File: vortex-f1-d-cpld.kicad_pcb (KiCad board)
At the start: 2 copper layers, 80 x 50 mm, 46 parts, among them J1 JTAG, U1 FDC 9229, U2 XC9572XL, U3 AZ1117-3.3, U4 uPD765AC, U5 AM29F010, U6 74LS06N, U7 SN74LS07N, U8 74LS06N, X1 8Mhz

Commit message: tweaks
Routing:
- net A0: track 91.3 -> 92.6 mm
- net WGATE: track 30.8 -> 31.3 mm
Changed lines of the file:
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@@
   (segment (start 148.69163 133.2072) (end 148.321644 132.837214) (width 0.2) (layer "F.Cu") (net 12))
   (segment (start 169.1386 137.3378) (end 168.8846 137.0838) (width 0.2) (layer "F.Cu") (net 12))
-  (segment (start 170.688 115.1128) (end 178.3588 115.1128) (width 0.2) (layer "F.Cu") (net 12))
-  (segment (start 170.2562 115.5446) (end 170.688 115.1128) (width 0.2) (layer "F.Cu") (net 12))
-  (segment (start 178.3588 115.1128) (end 178.6382 114.8334) (width 0.2) (layer "F.Cu") (net 12))
   (segment (start 148.321644 132.837214) (end 129.586014 132.837214) (width 0.2) (layer "F.Cu") (net 12))
   (segment (start 168.8846 137.0838) (end 165.9382 137.0838) (width 0.2) (layer "F.Cu") (net 12))
   (segment (start 163.108248 133.2072) (end 148.69163 133.2072) (width 0.2) (layer "F.Cu") (net 12))
+  (segment (start 178.4008 115.0708) (end 178.6382 114.8334) (width 0.2) (layer "F.Cu") (net 12))
+  (segment (start 169.3926 114.7572) (end 169.5784 114.5714) (width 0.2) (layer "F.Cu") (net 12))
+  (segment (start 176.660552 115.0708) (end 178.4008 115.0708) (width 0.2) (layer "F.Cu") (net 12))
+  (segment (start 176.161152 114.5714) (end 176.660552 115.0708) (width 0.2) (layer "F.Cu") (net 12))
   (segment (start 165.603 137.419) (end 165.603 138.171) (width 0.2) (layer "F.Cu") (net 12))
+  (segment (start 169.5784 114.5714) (end 176.161152 114.5714) (width 0.2) (layer "F.Cu") (net 12))
   (segment (start 168.548 133.458) (end 163.359048 133.458) (width 0.2) (layer "F.Cu") (net 12))
   (segment (start 165.9382 137.0838) (end 165.603 137.419) (width 0.2) (layer "F.Cu") (net 12))
@@
   (via (at 178.6382 114.8334) (size 0.5) (drill 0.3) (layers "F.Cu" "B.Cu") (net 12))
   (via (at 169.037 132.969) (size 0.5) (drill 0.3) (layers "F.Cu" "B.Cu") (net 12))
-  (via (at 170.2562 115.5446) (size 0.5) (drill 0.3) (layers "F.Cu" "B.Cu") (net 12))
+  (via (at 169.3926 114.7572) (size 0.5) (drill 0.3) (layers "F.Cu" "B.Cu") (net 12))
   (segment (start 178.158 108.096308) (end 178.457908 107.7964) (width 0.2) (layer "B.Cu") (net 12))
   (segment (start 178.457908 107.7964) (end 179.1225 107.7964) (width 0.2) (layer "B.Cu") (net 12))
-  (segment (start 170.2562 115.5446) (end 169.127242 116.673558) (width 0.2) (layer "B.Cu") (net 12))
   (segment (start 169.0878 133.0198) (end 169.037 132.969) (width 0.2) (layer "B.Cu") (net 12))
   (segment (start 178.158 108.496492) (end 178.158 108.096308) (width 0.2) (layer "B.Cu") (net 12))
-  (segment (start 169.691704 132.288896) (end 169.2402 132.7404) (width 0.2) (layer "B.Cu") (net 12))
+  (segment (start 169.472 124.89904) (end 169.472 125.869488) (width 0.2) (layer "B.Cu") (net 12))
   (segment (start 178.5398 108.878292) (end 178.158 108.496492) (width 0.2) (layer "B.Cu") (net 12))
-  (segment (start 169.472 124.89904) (end 169.472 125.869488) (width 0.2) (layer "B.Cu") (net 12))
+  (segment (start 169.3926 114.7572) (end 169.127242 115.022558) (width 0.2) (layer "B.Cu") (net 12))
+  (segment (start 169.691704 126.089192) (end 169.691704 132.288896) (width 0.2) (layer "B.Cu") (net 12))
+  (segment (start 169.127242 117.209642) (end 169.320242 117.402642) (width 0.2) (layer "B.Cu") (net 12))
+  (segment (start 169.320242 117.402642) (end 169.320242 124.747282) (width 0.2) (layer "B.Cu") (net 12))
+  (segment (start 169.472 125.869488) (end 169.691704 126.089192) (width 0.2) (layer "B.Cu") (net 12))
   (segment (start 169.2402 132.7404) (end 169.2402 133.0198) (width 0.2) (layer "B.Cu") (net 12))
   (segment (start 169.3316 137.1448) (end 169.3316 136.116848) (width 0.2) (layer "B.Cu") (net 12))
   (segment (start 178.5398 114.735) (end 178.5398 108.878292) (width 0.2) (layer "B.Cu") (net 12))
-  (segment (start 169.127242 116.673558) (end 169.127242 117.209642) (width 0.2) (layer "B.Cu") (net 12))
-  (segment (start 169.320242 124.747282) (end 169.472 124.89904) (width 0.2) (layer "B.Cu") (net 12))
   (segment (start 178.6382 114.8334) (end 178.5398 114.735) (width 0.2) (layer "B.Cu") (net 12))
   (segment (start 178.4096 115.062) (end 178.4096 116.8146) (width 0.2) (layer "B.Cu") (net 12))
   (segment (start 169.3316 136.116848) (end 169.2402 136.025448) (width 0.2) (layer "B.Cu") (net 12))
+  (segment (start 169.691704 132.288896) (end 169.2402 132.7404) (width 0.2) (layer "B.Cu") (net 12))
   (segment (start 178.4096 116.8146) (end 179.3494 117.7544) (width 0.2) (layer "B.Cu") (net 12))
   (segment (start 169.2402 136.025448) (end 169.2402 133.0198) (width 0.2) (layer "B.Cu") (net 12))
@@
   (segment (start 169.1386 137.3378) (end 169.3316 137.1448) (width 0.2) (layer "B.Cu") (net 12))
   (segment (start 169.2402 133.0198) (end 169.0878 133.0198) (width 0.2) (layer "B.Cu") (net 12))
-  (segment (start 169.320242 117.402642) (end 169.320242 124.747282) (width 0.2) (layer "B.Cu") (net 12))
-  (segment (start 169.127242 117.209642) (end 169.320242 117.402642) (width 0.2) (layer "B.Cu") (net 12))
-  (segment (start 169.472 125.869488) (end 169.691704 126.089192) (width 0.2) (layer "B.Cu") (net 12))
-  (segment (start 169.691704 126.089192) (end 169.691704 132.288896) (width 0.2) (layer "B.Cu") (net 12))
+  (segment (start 169.127242 115.022558) (end 169.127242 117.209642) (width 0.2) (layer "B.Cu") (net 12))
+  (segment (start 169.320242 124.747282) (end 169.472 124.89904) (width 0.2) (layer "B.Cu") (net 12))
   (segment (start 133.6682 136.767) (end 154.307 136.767) (width 0.2) (layer "F.Cu") (net 13))
   (segment (start 133.4516 136.5504) (end 133.6682 136.767) (width 0.2) (layer "F.Cu") (net 13))
@@
   (segment (start 187.695265 107.576588) (end 187.2964 107.177723) (width 0.2) (layer "B.Cu") (net 89))
   (segment (start 187.5822 105.48704) (end 187.5822 100.0168) (width 0.2) (layer "B.Cu") (net 89))
-  (segment (start 173.7614 110.744) (end 174.0274 110.478) (width 0.2) (layer "F.Cu") (net 90))
-  (segment (start 181.1528 109.9852) (end 186.085892 109.9852) (width 0.2) (layer "F.Cu") (net 90))
-  (segment (start 171.908408 110.744) (end 173.7614 110.744) (width 0.2) (layer "F.Cu") (net 90))
-  (segment (start 168.939395 111.601531) (end 169.239516 111.901652) (width 0.2) (layer "F.Cu") (net 90))
-  (segment (start 169.239516 111.901652) (end 170.4848 111.901652) (width 0.2) (layer "F.Cu") (net 90))
-  (segment (start 170.4848 111.901652) (end 170.774948 111.901652) (width 0.2) (layer "F.Cu") (net 90))
-  (segment (start 186.085892 109.9852) (end 187.283217 108.787875) (width 0.2) (layer "F.Cu") (net 90))
-  (segment (start 171.5262 111.1504) (end 171.5262 111.126208) (width 0.2) (layer "F.Cu") (net 90))
-  (segment (start 180.479192 110.478) (end 180.971992 109.9852) (width 0.2) (layer "F.Cu") (net 90))
-  (segment (start 171.5262 111.126208) (end 171.908408 110.744) (width 0.2) (layer "F.Cu") (net 90))
-  (segment (start 170.774948 111.901652) (end 171.5262 111.1504) (width 0.2) (layer "F.Cu") (net 90))
-  (segment (start 174.0274 110.478) (end 180.479192 110.478) (width 0.2) (layer "F.Cu") (net 90))
-  (segment (start 180.971992 109.9852) (end 181.1528 109.9852) (width 0.2) (layer "F.Cu") (net 90))
+  (segment (start 175.135848 110.1622) (end 169.441 110.1622) (width 0.2) (layer "F.Cu") (net 90))
+  (segment (start 175.141448 110.1566) (end 175.135848 110.1622) (width 0.2) (layer "F.Cu") (net 90))
+  (segment (start 169.441 110.1622) (end 168.939395 110.663805) (width 0.2) (layer "F.Cu") (net 90))
+  (segment (start 186.085892 109.9852) (end 180.971992 109.9852) (width 0.2) (layer "F.Cu") (net 90))
+  (segment (start 180.971992 109.9852) (end 180.505992 110.4512) (width 0.2) (layer "F.Cu") (net 90))
+  (segment (start 180.505992 110.4512) (end 177.762408 110.4512) (width 0.2) (layer "F.Cu") (net 90))
+  (segment (start 177.467808 110.1566) (end 175.141448 110.1566) (width 0.2) (layer "F.Cu") (net 90))
+  (segment (start 187.283217 108.787875) (end 186.085892 109.9852) (width 0.2) (layer "F.Cu") (net 90))
+  (segment (start 168.939395 110.663805) (end 168.939395 111.601531) (width 0.2) (layer "F.Cu") (net 90))
+  (segment (start 177.762408 110.4512) (end 177.467808 110.1566) (width 0.2) (layer "F.Cu") (net 90))
   (via (at 187.283217 108.787875) (size 0.5) (drill 0.3) (layers "F.Cu" "B.Cu") (net 90))
   (via (at 168.939395 111.601531) (size 0.5) (drill 0.3) (layers "F.Cu" "B.Cu") (net 90))

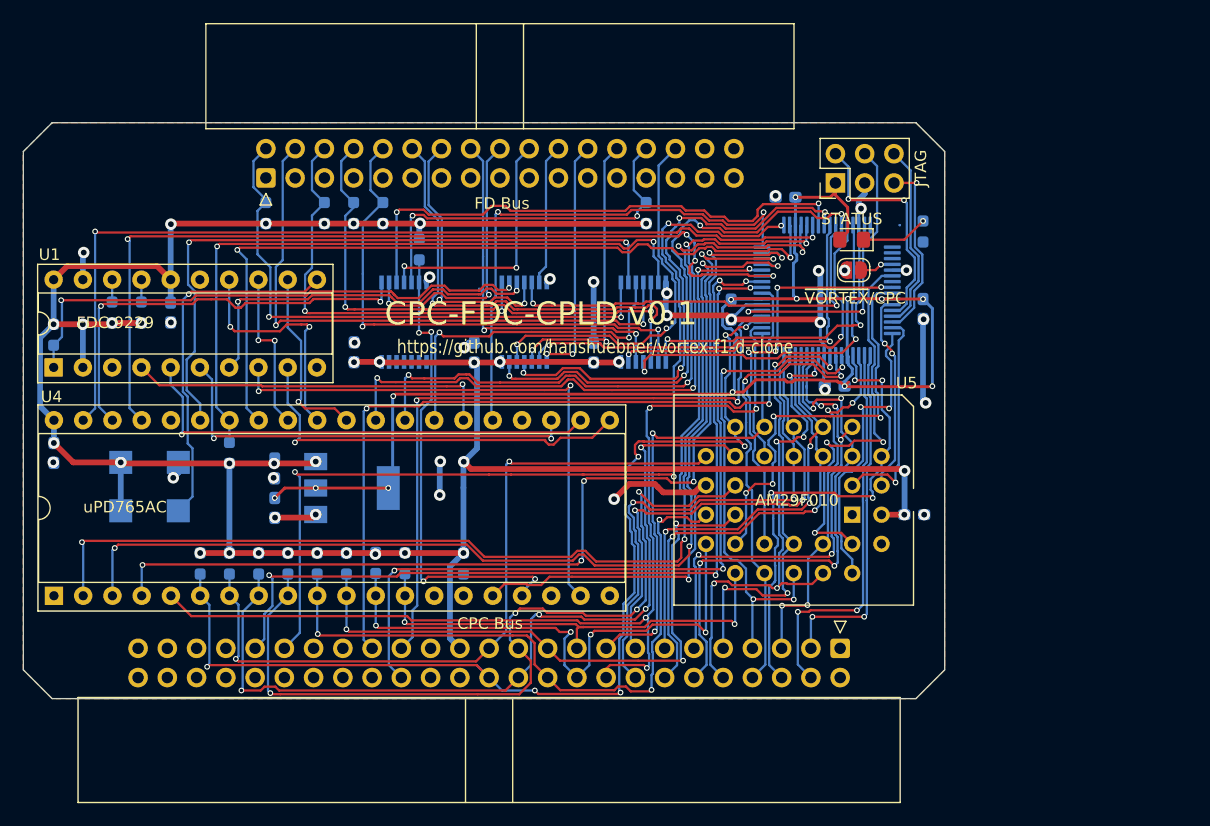
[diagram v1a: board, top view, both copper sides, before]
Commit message: Layout with ROM redone
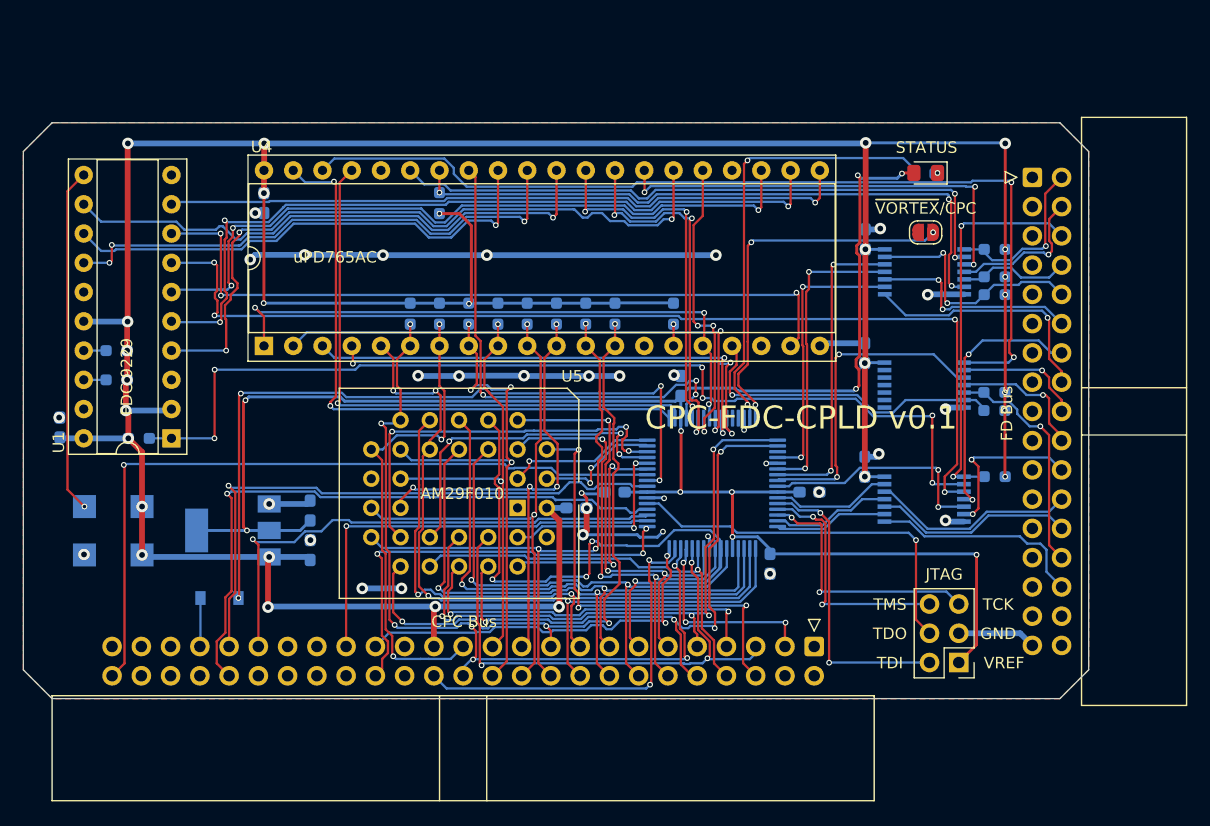
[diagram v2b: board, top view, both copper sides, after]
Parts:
- added D1: 1N4148W, Diode_SMD:D_SOD-123, B.Cu at (132.0, 131.3)
- moved S2 66.5 mm to (202.6, 94.7), turned to 0 degrees
- moved R16 63.4 mm to (199.3, 101.0), turned to 0 degrees
- moved R17 62.5 mm to (199.3, 120.7), turned to 0 degrees
- moved R18 55.9 mm to (199.3, 103.4), turned to 0 degrees
- moved R19 53.6 mm to (199.3, 104.9), turned to 0 degrees
- moved R15 51.9 mm to (199.3, 115.0), turned to 0 degrees
- moved U8 45.5 mm to (193.2, 112.8), turned to 180 degrees
- moved C9 45.5 mm to (188.1, 100.1)
- moved J1 43.0 mm to (196.2, 136.9), turned to 180 degrees
- moved U7 38.0 mm to (193.2, 122.7), turned to 180 degrees
- moved R20 34.0 mm to (199.3, 113.4), turned to 0 degrees
- moved C8 33.9 mm to (188.1, 110.0)
- moved C6 31.1 mm to (166.3, 122.1), turned to 180 degrees
- moved C12 29.3 mm to (163.0, 123.4)
- moved U5 29.1 mm to (157.9, 123.4)
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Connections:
- S1 pad 10: /A8 -> A8
- S1 pad 28: /~{MREQ} -> ~{MREQ}
- S1 pad 42: /~{ROMEN} -> ~{ROMEN}
- S1 pad 43: /ROMDIS -> ROMDIS
- S1 pad 50: /CLK4 -> CLK4
- S1 pad 9: /A9 -> A9
- U2 pad 1: READY -> ~{RW}/SEEK
- U2 pad 10: ~{DS2'} -> ~{IOWR}
- U2 pad 11: ~{DS3'} -> ~{FDCCS}
- U2 pad 12: STEP -> unconnected-(U2-Pad12)
- U2 pad 13: WGATE -> unconnected-(U2-Pad13)
- U2 pad 15: TRK00 -> LED1
- U2 pad 16: LED1 -> ~{VORTEX}/CPC
- U2 pad 17: unconnected-(U2-Pad17) -> A9
- U2 pad 18: unconnected-(U2-Pad18) -> A8
- U2 pad 2: FLT/TRK0 -> FLTR/STEP
- U2 pad 20: ~{VORTEX}/CPC -> STEP
- U2 pad 22: ~{ROMWE} -> WGATE
- U2 pad 23: LED2 -> TRK00
- U2 pad 24: ~{ROMOE} -> MTRON
- U2 pad 25: ~{ROMCE} -> ~{DS2'}
- U2 pad 27: ROMA16 -> ~{DS1'}
- U2 pad 31: ROMA15 -> ~{DS0'}
- U2 pad 32: ROMA14 -> ~{DS3'}
- U2 pad 33: /A15 -> A0
- U2 pad 34: /A14 -> /A1
- U2 pad 35: /A13 -> /A2
- U2 pad 36: /A12 -> /A3
- U2 pad 38: /A11 -> /A4
- U2 pad 39: /A10 -> /A5
- U2 pad 4: US0 -> FLT/TRK0
- U2 pad 40: /A9 -> /A6
- U2 pad 42: /A8 -> /A7
- U2 pad 43: /A7 -> /A10
- U2 pad 44: /A6 -> /A13
- U2 pad 45: /A5 -> /A15
- U2 pad 46: /A4 -> D0
- U2 pad 47: /A3 -> ~{MREQ}
- U2 pad 48: /A2 -> ~{IORQ}
- U2 pad 49: /A1 -> ~{RD}
- U2 pad 50: A0 -> ~{WR}
- U2 pad 51: D0 -> READY
- U2 pad 52: ~{IORQ} -> ~{ROMEN}
- U2 pad 56: ~{WR} -> ~{RSET}
- U2 pad 57: ~{RD} -> Net-(D1-Pad2)
- U2 pad 58: ~{RSET} -> CLK4
- U2 pad 59: FLTR/STEP -> ROMA14
- U2 pad 6: ~{RW}/SEEK -> US0
- U2 pad 60: ~{IORD} -> ~{ROMWE}
- U2 pad 61: ~{IOWR} -> ~{ROMOE}
- U2 pad 62: RESET -> ~{ROMCE}
- U2 pad 63: ~{FDCCS} -> ROMA16
- U2 pad 64: WE -> ROMA15
- U2 pad 7: MTRON -> WE
- U2 pad 8: ~{DS0'} -> RESET
- U2 pad 9: ~{DS1'} -> ~{IORD}
- U5 pad 26: /A9 -> A9
- U5 pad 27: /A8 -> A8
- U6 pad 12: ~{STEP} -> TRK00
- U6 pad 13: STEP -> ~{TRK00}
- U6 pad 8: TRK00 -> ~{STEP}
- U6 pad 9: ~{TRK00} -> STEP
- U7 pad 12: ~{DS3} -> ~{DS1}
- U7 pad 13: ~{DS3'} -> ~{DS1'}
- U7 pad 8: ~{DS1} -> ~{DS3}
- U7 pad 9: ~{DS1'} -> ~{DS3'}
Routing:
- net +5V: track 239.9 -> 307.9 mm, vias 34 -> 28
- net CLK4: track 0.00 -> 64.7 mm, vias 0 -> 1
- net Net-(D1-Pad2): track 0.00 -> 64.5 mm, vias 0 -> 4
- net WDATA': track 32.6 -> 90.3 mm, vias 2 -> 4
- net A9: track 0.00 -> 55.3 mm, vias 0 -> 4
- net ~{ROMEN}: track 0.00 -> 53.7 mm, vias 0 -> 1
- net A8: track 0.00 -> 53.2 mm, vias 0 -> 4
- net ~{IOWR}: track 91.0 -> 43.3 mm, vias 4 -> 2
- net /A8: track 44.8 -> 0.00 mm, vias 6 -> 0
- net ~{FDCCS}: track 87.3 -> 42.6 mm, vias 6 -> 3
- net DIR: track 37.4 -> 81.8 mm
- net ~{IORD}: track 89.8 -> 47.5 mm, vias 4 -> 2
- net ~{SIDE1}: track 51.9 -> 12.9 mm, vias 2 -> 1
- net RDATA': track 47.4 -> 86.3 mm, vias 2 -> 6
- net /A9: track 38.8 -> 0.00 mm, vias 4 -> 0
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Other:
- board size 80 x 50 mm -> 92.5 x 50 mm
- board text added: "GND"
- board text added: "TCK"
- board text added: "TDI"
- board text added: "TDO"
- board text added: "TMS"
- board text added: "VREF"
